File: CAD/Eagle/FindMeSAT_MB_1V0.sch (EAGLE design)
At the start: 124 parts, among them IC1111 LM2831YMF, J291 MCX-J-P-X-RA-SM1, J701 MOLEX_105017-0001, J801 MICROSIM-8P_SDCARD-8P_MOLEX-1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, J901 JST_S3B-XH-A, Q101 ABS07, Q651 ABM3B-16MHZ-10-R50-1-U, U1001 CFPT-141, U101 ATXMEGA256A3BU-AU, U1011 OPA354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

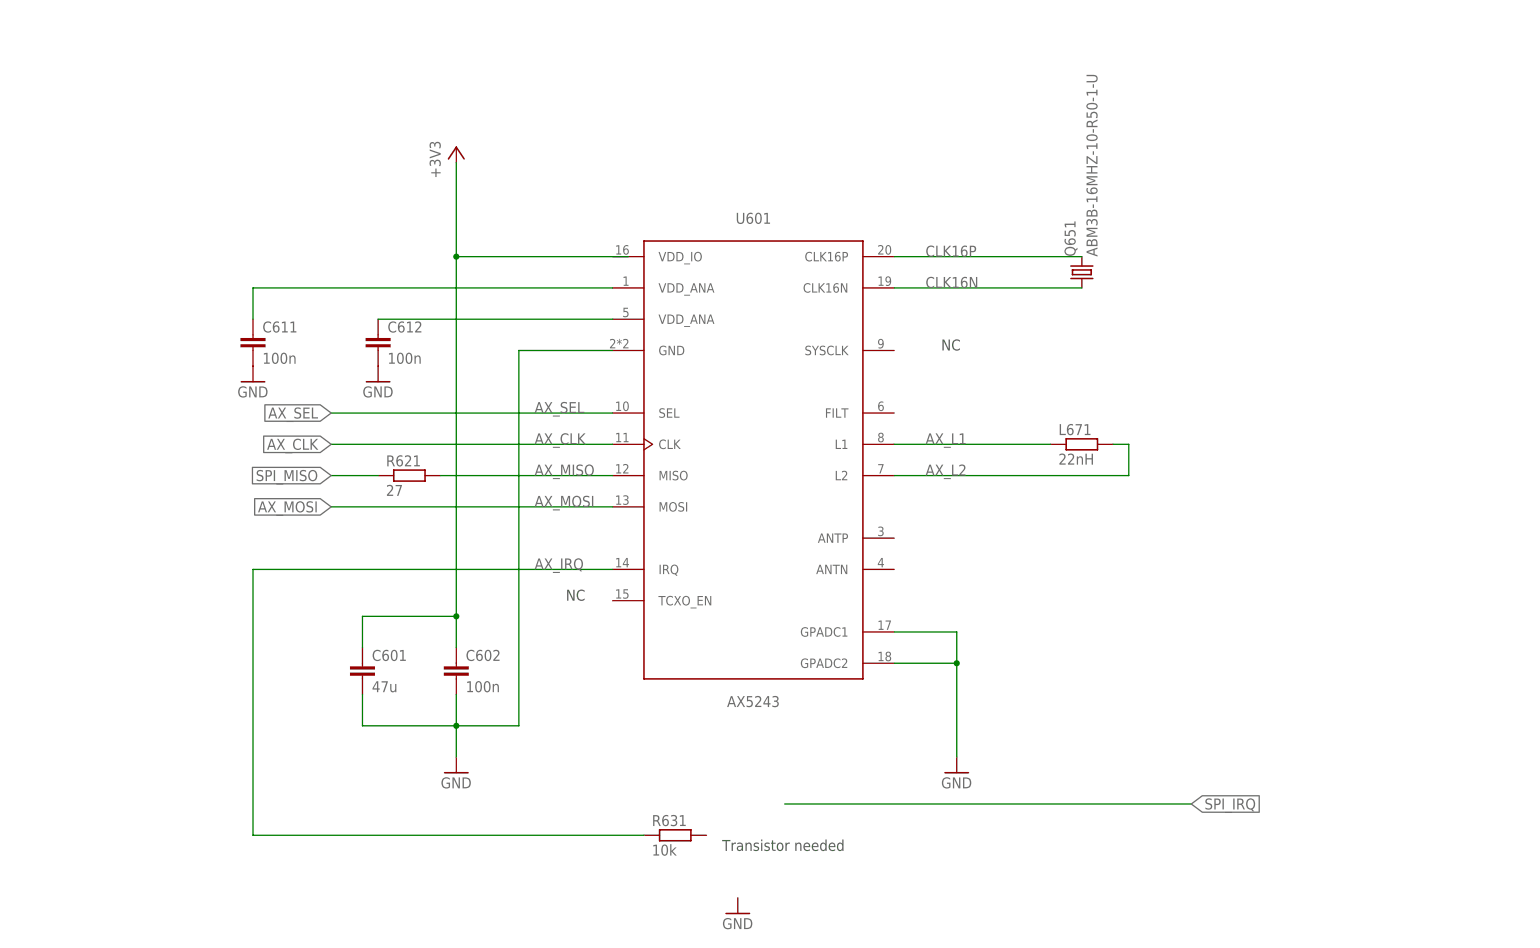
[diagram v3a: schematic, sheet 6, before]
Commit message: Eagle - AX5243 placed and some routes are made - before SPI routing
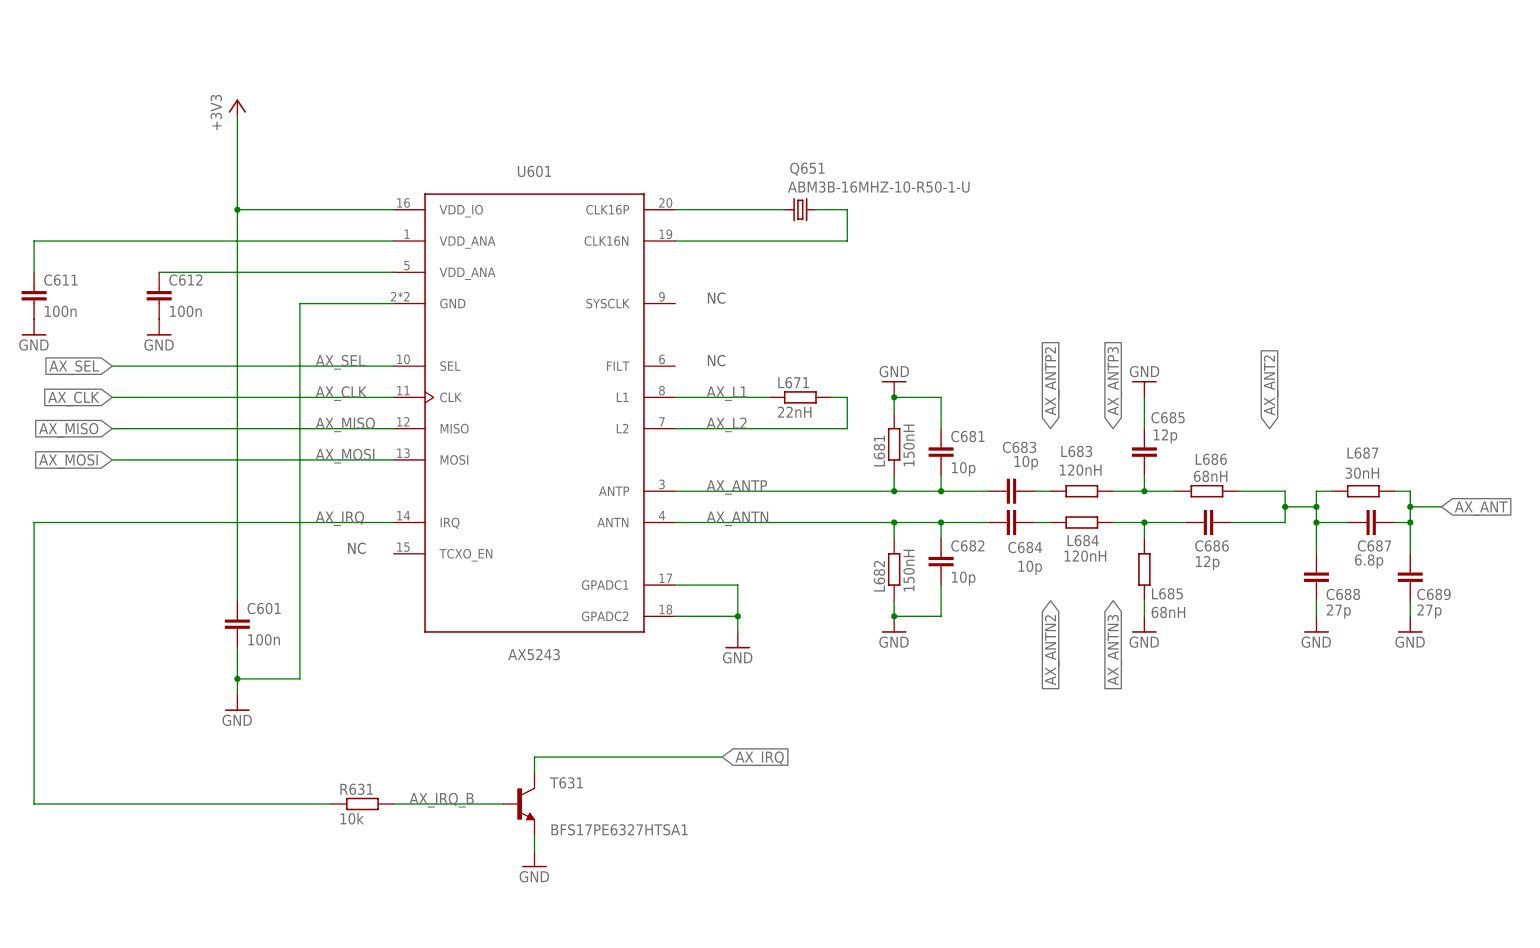
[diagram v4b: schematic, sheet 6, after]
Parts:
- removed C602: 100n, rcl:C-EUC0603
- removed R621: 27, rcl:R-EU_R0603
- added C681, C682, C683, C684: 10p, rcl:C-EUC0603
- added C685, C686: 12p, rcl:C-EUC0603
- added C687: 6.8p, rcl:C-EUC0603
- added C688, C689: 27p, rcl:C-EUC0603
- added L681, L682: 150nH, rcl:R-EU_R0603
- added L683, L684: 120nH, rcl:R-EU_R0603
- added L685, L686: 68nH, rcl:R-EU_R0603
- added L687: 30nH, rcl:R-EU_R0603
- added T631: BFS17PE6327HTSA1, df4iah_bipoltransistor:BFS17PE6327HTSA1
- C601: value 47u -> 100n
- R722, R723, R725: device rcl:R-EU_R0805 -> rcl:R-EU_R0603
- U301: value MPU-9250 -> 9DoF IMU
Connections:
- net N$1 renamed VDD_ANA@1
- removed net SPI_MISO: R621.1
- new net AX_ANT: C687.2, C689.1, L687.2
- new net AX_ANT2: C686.2, C687.1, C688.1, L686.2, L687.1
- new net AX_ANTN: C682.1, C684.1, L682.2, U601.ANTN
- new net AX_ANTN2: C684.2, L684.1
- new net AX_ANTN3: C686.1, L684.2, L685.2
- new net AX_ANTP: C681.2, C683.1, L681.1, U601.ANTP
- new net AX_ANTP2: C683.2, L683.1
- new net AX_ANTP3: C685.2, L683.2, L686.1
- new net AX_IRQ_B: R631.2, T631.B
- net +3V3: now also U601.VDD_IO; no longer C602.1
- net AX_CLK: now also U101A.PC7
- net AX_IRQ: now also T631.C, U101A.PC3
- net AX_MISO: now also U101A.PC6; no longer R621.2
- net AX_MOSI: now also U101A.PC5
- net AX_SEL: now also U101A.PC4
- net CLK16N: now also Q651.2; no longer Q651.1
- net CLK16P: now also Q651.1; no longer Q651.2
- net GND: now also C681.1, C682.2, C685.1, C688.2, C689.2, L681.2, L682.1, L685.1, T631.E; no longer C602.2
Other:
- note removed: "Transistor needed"
- moved on the sheet: C601, C611, C612, L671, Q651, R631, U601

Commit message: Eagle - before CPU block movement one by left
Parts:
- removed C681, C682, C683, C684: 10p, rcl:C-EUC0603
- removed C687: 6.8p, rcl:C-EUC0603
- removed C688, C689: 27p, rcl:C-EUC0603
- removed L682: 150nH, rcl:R-EU_R0603
- removed L683, L684: 120nH, rcl:R-EU_R0603
- removed L687: 30nH, rcl:R-EU_R0603
- removed R631: 10k, rcl:R-EU_R0603
- removed T631: BFS17PE6327HTSA1, df4iah_bipoltransistor:BFS17PE6327HTSA1
- added J681: SMA_CON, df4iah_connector:SMA_SMT_AMPHENOL-901-143
- C685: value 12p -> 22p
- C686: value 12p -> 15p
- L685, L686: value 68nH -> 82nH
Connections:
- removed net AX_ANT2: C686.2, C687.1, C688.1, L686.2, L687.1
- removed net AX_ANTN2: C684.2, L684.1
- removed net AX_ANTN3: C686.1, L684.2, L685.2
- removed net AX_ANTP2: C683.2, L683.1
- removed net AX_ANTP3: C685.2, L683.2, L686.1
- removed net AX_IRQ_B: R631.2, T631.B
- net AX_ANT: now also C686.2, J681.1, L686.2; no longer C687.2, C689.1, L687.2
- net AX_ANTN: now also C686.1, L685.2; no longer C682.1, C684.1, L682.2
- net AX_ANTP: now also C685.2, L686.1; no longer C681.2, C683.1
- net AX_IRQ: no longer R631.1, T631.C
- net GND: now also J681.2; no longer C681.1, C682.2, C688.2, C689.2, L682.1, T631.E
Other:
- moved on the sheet: C601, C685, C686, L681, L685, L686

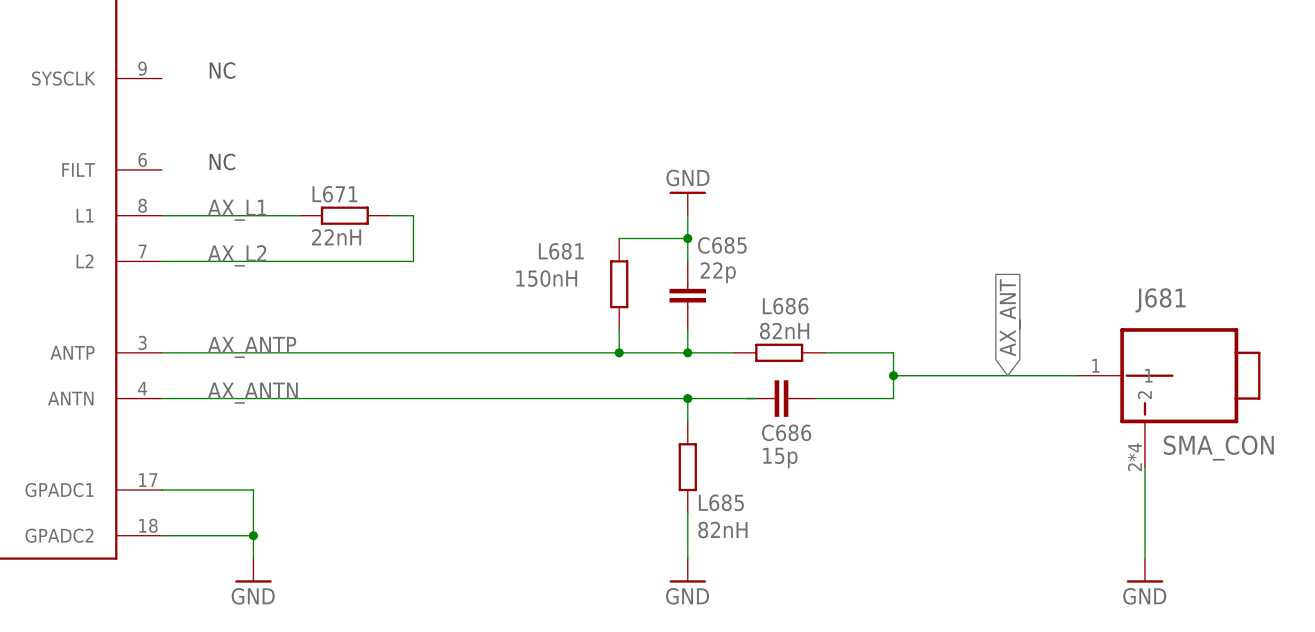
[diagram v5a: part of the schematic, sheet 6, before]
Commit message: Eagle - more fine tuning after CPU block movement done
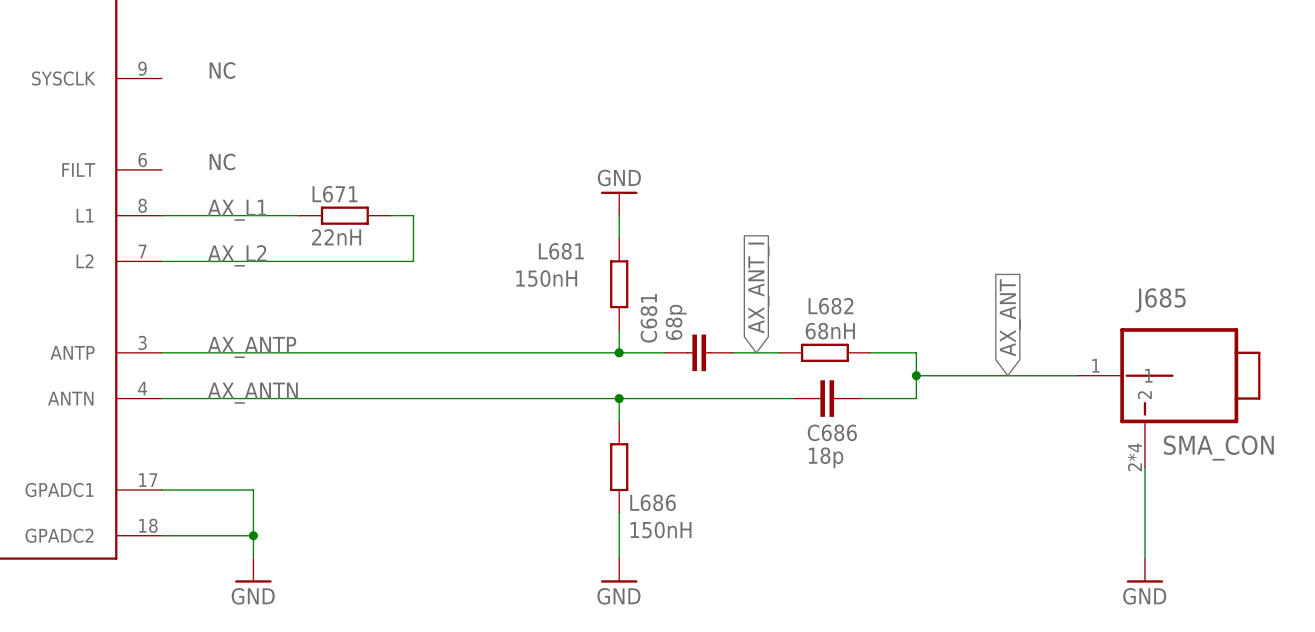
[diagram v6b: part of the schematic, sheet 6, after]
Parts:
- removed C685: 22p, rcl:C-EUC0603
- removed L685: 82nH, rcl:R-EU_R0603
- added C681: 68p, rcl:C-EUC0603
- added L682: 68nH, rcl:R-EU_R0603
- C686: value 15p -> 18p
- L686: value 82nH -> 150nH
- renumbered J681 to J685
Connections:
- new net AX_ANT_I: C681.2, L682.1
- net AX_ANT: now also L682.2; no longer L686.2
- net AX_ANTN: now also L686.2; no longer L685.2
- net AX_ANTP: now also C681.1; no longer C685.2, L686.1
- net GND: now also L686.1; no longer C685.1, L685.1
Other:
- moved on the sheet: C686, L686
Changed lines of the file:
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@@
 <part name="Q651" library="adafruit" deviceset="CRYSTAL" device="CTS406" value="ABM3B-16MHZ-10-R50-1-U"/>
 <part name="L671" library="rcl" deviceset="R-EU_" device="R0603" value="22nH"/>
-<part name="C685" library="rcl" deviceset="C-EU" device="C0603" value="22p"/>
+<part name="C681" library="rcl" deviceset="C-EU" device="C0603" value="68p"/>
 <part name="GND683" library="df4iah_supply" deviceset="GND" device=""/>
-<part name="L685" library="rcl" deviceset="R-EU_" device="R0603" value="82nH"/>
-<part name="L686" library="rcl" deviceset="R-EU_" device="R0603" value="82nH"/>
+<part name="L686" library="rcl" deviceset="R-EU_" device="R0603" value="150nH"/>
+<part name="L682" library="rcl" deviceset="R-EU_" device="R0603" value="68nH"/>
 <part name="GND684" library="df4iah_supply" deviceset="GND" device=""/>
-<part name="C686" library="rcl" deviceset="C-EU" device="C0603" value="15p"/>
+<part name="C686" library="rcl" deviceset="C-EU" device="C0603" value="18p"/>
 <part name="L681" library="rcl" deviceset="R-EU_" device="R0603" value="150nH"/>
-<part name="J681" library="df4iah_connector" deviceset="SMA_SMT_AMPHENOL-901-143" device="" value="SMA_CON"/>
+<part name="J685" library="df4iah_connector" deviceset="SMA_SMT_AMPHENOL-901-143" device="" value="SMA_CON"/>
 <part name="GND689" library="df4iah_supply" deviceset="GND" device=""/>
 </parts>
@@
 </instance>
 <instance part="L671" gate="G$1" x="137.16" y="104.14"/>
-<instance part="C685" gate="G$1" x="175.26" y="96.52" smashed="yes">
-<attribute name="NAME" x="176.276" y="99.949" size="1.778" layer="95"/>
-<attribute name="VALUE" x="176.53" y="97.155" size="1.778" layer="96"/>
+<instance part="C681" gate="G$1" x="175.26" y="88.9" smashed="yes" rot="R90">
+<attribute name="NAME" x="171.831" y="89.916" size="1.778" layer="95" rot="R90"/>
+<attribute name="VALUE" x="174.625" y="90.17" size="1.778" layer="96" rot="R90"/>
 </instance>
-<instance part="GND683" gate="1" x="175.26" y="106.68" rot="R180"/>
-<instance part="L685" gate="G$1" x="175.26" y="76.2" smashed="yes" rot="R90">
-<attribute name="NAME" x="176.276" y="71.3486" size="1.778" layer="95"/>
-<attribute name="VALUE" x="176.276" y="68.326" size="1.778" layer="96"/>
+<instance part="GND683" gate="1" x="167.64" y="106.68" rot="R180"/>
+<instance part="L686" gate="G$1" x="167.64" y="76.2" smashed="yes" rot="R90">
+<attribute name="NAME" x="168.656" y="71.3486" size="1.778" layer="95"/>
+<attribute name="VALUE" x="168.656" y="68.326" size="1.778" layer="96"/>
 </instance>
-<instance part="L686" gate="G$1" x="185.42" y="88.9" smashed="yes">
-<attribute name="NAME" x="183.388" y="93.1926" size="1.778" layer="95"/>
-<attribute name="VALUE" x="183.134" y="90.424" size="1.778" layer="96"/>
+<instance part="L682" gate="G$1" x="190.5" y="88.9" smashed="yes">
+<attribute name="NAME" x="188.468" y="93.1926" size="1.778" layer="95"/>
+<attribute name="VALUE" x="188.214" y="90.424" size="1.778" layer="96"/>
 </instance>
-<instance part="GND684" gate="1" x="175.26" y="63.5"/>
-<instance part="C686" gate="G$1" x="184.404" y="83.82" smashed="yes" rot="R90">
-<attribute name="NAME" x="183.388" y="79.121" size="1.778" layer="95"/>
-<attribute name="VALUE" x="183.388" y="76.581" size="1.778" layer="96"/>
+<instance part="GND684" gate="1" x="167.64" y="63.5"/>
+<instance part="C686" gate="G$1" x="189.484" y="83.82" smashed="yes" rot="R90">
+<attribute name="NAME" x="188.468" y="79.121" size="1.778" layer="95"/>
+<attribute name="VALUE" x="188.468" y="76.581" size="1.778" layer="96"/>
 </instance>
 <instance part="L681" gate="G$1" x="167.64" y="96.52" smashed="yes" rot="R90">
@@
 <attribute name="VALUE" x="155.956" y="96.266" size="1.778" layer="96"/>
 </instance>
-<instance part="J681" gate="A" x="228.6" y="86.36"/>
+<instance part="J685" gate="A" x="228.6" y="86.36"/>
 <instance part="GND689" gate="1" x="226.06" y="63.5"/>
 </instances>
@@
 </segment>
 <segment>
+<pinref part="L681" gate="G$1" pin="2"/>
 <pinref part="GND683" gate="1" pin="GND"/>
-<pinref part="C685" gate="G$1" pin="1"/>
-<wire x1="175.26" y1="104.14" x2="175.26" y2="101.6" width="0.1524" layer="91"/>
-<pinref part="L681" gate="G$1" pin="2"/>
-<wire x1="175.26" y1="101.6" x2="175.26" y2="99.06" width="0.1524" layer="91"/>
-<wire x1="175.26" y1="101.6" x2="167.64" y2="101.6" width="0.1524" layer="91"/>
-<junction x="175.26" y="101.6"/>
-</segment>
-<segment>
-<pinref part="L685" gate="G$1" pin="1"/>
-<wire x1="175.26" y1="71.12" x2="175.26" y2="66.04" width="0.1524" layer="91"/>
+<wire x1="167.64" y1="104.14" x2="167.64" y2="101.6" width="0.1524" layer="91"/>
+</segment>
+<segment>
+<pinref part="L686" gate="G$1" pin="1"/>
+<wire x1="167.64" y1="71.12" x2="167.64" y2="66.04" width="0.1524" layer="91"/>
 <pinref part="GND684" gate="1" pin="GND"/>
 </segment>
 <segment>
 <pinref part="GND689" gate="1" pin="GND"/>
-<pinref part="J681" gate="A" pin="2"/>
+<pinref part="J685" gate="A" pin="2"/>
 <wire x1="226.06" y1="66.04" x2="226.06" y2="76.2" width="0.1524" layer="91"/>
 </segment>
@@
 <wire x1="116.84" y1="88.9" x2="167.64" y2="88.9" width="0.1524" layer="91"/>
 <label x="121.92" y="88.9" size="1.778" layer="95"/>
-<pinref part="L686" gate="G$1" pin="1"/>
-<pinref part="C685" gate="G$1" pin="2"/>
-<wire x1="167.64" y1="88.9" x2="175.26" y2="88.9" width="0.1524" layer="91"/>
-<wire x1="175.26" y1="88.9" x2="180.34" y2="88.9" width="0.1524" layer="91"/>
-<wire x1="175.26" y1="88.9" x2="175.26" y2="91.44" width="0.1524" layer="91"/>
-<junction x="175.26" y="88.9"/>
 <pinref part="L681" gate="G$1" pin="1"/>
 <wire x1="167.64" y1="88.9" x2="167.64" y2="91.44" width="0.1524" layer="91"/>
 <junction x="167.64" y="88.9"/>
+<pinref part="C681" gate="G$1" pin="1"/>
+<wire x1="167.64" y1="88.9" x2="172.72" y2="88.9" width="0.1524" layer="91"/>
 </segment>
 </net>
@@
 <segment>
 <pinref part="U601" gate="A" pin="ANTN"/>
-<wire x1="116.84" y1="83.82" x2="175.26" y2="83.82" width="0.1524" layer="91"/>
+<wire x1="116.84" y1="83.82" x2="167.64" y2="83.82" width="0.1524" layer="91"/>
 <label x="121.92" y="83.82" size="1.778" layer="95"/>
-<pinref part="L685" gate="G$1" pin="2"/>
-<wire x1="175.26" y1="83.82" x2="181.864" y2="83.82" width="0.1524" layer="91"/>
-<wire x1="181.864" y1="83.82" x2="182.88" y2="83.82" width="0.1524" layer="91"/>
-<wire x1="175.26" y1="83.82" x2="175.26" y2="81.28" width="0.1524" layer="91"/>
-<junction x="175.26" y="83.82"/>
+<pinref part="L686" gate="G$1" pin="2"/>
+<wire x1="167.64" y1="83.82" x2="186.944" y2="83.82" width="0.1524" layer="91"/>
+<wire x1="167.64" y1="83.82" x2="167.64" y2="81.28" width="0.1524" layer="91"/>
+<junction x="167.64" y="83.82"/>
 <pinref part="C686" gate="G$1" pin="1"/>
 </segment>
@@
 <segment>
 <label x="210.82" y="86.36" size="1.778" layer="95" rot="R90" xref="yes"/>
-<pinref part="L686" gate="G$1" pin="2"/>
+<pinref part="L682" gate="G$1" pin="2"/>
 <pinref part="C686" gate="G$1" pin="2"/>
-<wire x1="189.484" y1="83.82" x2="198.12" y2="83.82" width="0.1524" layer="91"/>
-<wire x1="198.12" y1="83.82" x2="198.12" y2="86.36" width="0.1524" layer="91"/>
-<wire x1="198.12" y1="86.36" x2="198.12" y2="88.9" width="0.1524" layer="91"/>
-<wire x1="198.12" y1="88.9" x2="190.5" y2="88.9" width="0.1524" layer="91"/>
-<junction x="198.12" y="86.36"/>
-<wire x1="218.44" y1="86.36" x2="198.12" y2="86.36" width="0.1524" layer="91"/>
-<pinref part="J681" gate="A" pin="1"/>
+<wire x1="194.564" y1="83.82" x2="200.66" y2="83.82" width="0.1524" layer="91"/>
+<wire x1="200.66" y1="83.82" x2="200.66" y2="86.36" width="0.1524" layer="91"/>
+<wire x1="200.66" y1="86.36" x2="200.66" y2="88.9" width="0.1524" layer="91"/>
+<wire x1="200.66" y1="88.9" x2="195.58" y2="88.9" width="0.1524" layer="91"/>
+<junction x="200.66" y="86.36"/>
+<wire x1="218.44" y1="86.36" x2="200.66" y2="86.36" width="0.1524" layer="91"/>
+<pinref part="J685" gate="A" pin="1"/>
 </segment>
 </net>
@@
 </segment>
 </net>
+<net name="AX_ANT_I" class="2">
+<segment>
+<pinref part="C681" gate="G$1" pin="2"/>
+<pinref part="L682" gate="G$1" pin="1"/>
+<wire x1="180.34" y1="88.9" x2="185.42" y2="88.9" width="0.1524" layer="91"/>
+<label x="182.88" y="88.9" size="1.778" layer="95" rot="R90" xref="yes"/>
+</segment>
+</net>
